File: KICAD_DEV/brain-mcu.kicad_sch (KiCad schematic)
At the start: 21 parts, among them SW1 SW_Push, SW2 SW_Push, U1 STM32H743VITx, Y1 8 MHz, Y2 32.768 KHz

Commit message: cleaning stuff up!
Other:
- note added: "IIf this SoC get's full, feel free to add a new one (just not too big!)"
- note added: "Please create a new hierarchial sheet in the root schematic, not this one if you're adding stuff!"
- note added: "Please don't alter anything aside from the GPIO's!"
- moved on the sheet: C10, C21, C23, C24, C25, C26, C27, C28, C29, C30, C31, C9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

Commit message: added all the basic footprints!
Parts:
- C10, C21, C23, C24, C25, C26, C27, C28, C29, C30, C31, C7, C8: footprint (none) -> Capacitor_SMD:C_0402_1005Metric
- C9: footprint (none) -> Capacitor_SMD:C_0603_1608Metric
- R13, R14: footprint (none) -> Resistor_SMD:R_0402_1005Metric
- SW1, SW2: footprint (none) -> Button_Switch_SMD:SW_Push_SPST_NO_Alps_SKRK
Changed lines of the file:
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@@
 			)
 		)
-		(property "Footprint" ""
+		(property "Footprint" "Capacitor_SMD:C_0603_1608Metric"
 			(at 55.5752 68.58 0)
 			(effects
@@
 			)
 		)
-		(property "Footprint" ""
+		(property "Footprint" "Capacitor_SMD:C_0402_1005Metric"
 			(at 77.1652 111.76 0)
 			(effects
@@
 			)
 		)
-		(property "Footprint" ""
+		(property "Footprint" "Capacitor_SMD:C_0402_1005Metric"
 			(at 192.7352 218.44 0)
 			(effects
@@
 			)
 		)
-		(property "Footprint" ""
+		(property "Footprint" "Button_Switch_SMD:SW_Push_SPST_NO_Alps_SKRK"
 			(at 68.58 97.79 0)
 			(effects
@@
 			)
 		)
-		(property "Footprint" ""
+		(property "Footprint" "Capacitor_SMD:C_0402_1005Metric"
 			(at 86.0552 68.58 0)
 			(effects
@@
 			)
 		)
-		(property "Footprint" ""
+		(property "Footprint" "Capacitor_SMD:C_0402_1005Metric"
 			(at 86.36 181.9148 0)
 			(effects
@@
 			)
 		)
-		(property "Footprint" ""
+		(property "Footprint" "Capacitor_SMD:C_0402_1005Metric"
 			(at 86.36 208.5848 0)
 			(effects
@@
 			)
 		)
-		(property "Footprint" ""
+		(property "Footprint" "Capacitor_SMD:C_0402_1005Metric"
 			(at 86.36 216.2048 0)
 			(effects
@@
 			)
 		)
-		(property "Footprint" ""
+		(property "Footprint" "Resistor_SMD:R_0402_1005Metric"
 			(at 74.422 143.51 90)
 			(effects
@@
 			)
 		)
-		(property "Footprint" ""
+		(property "Footprint" "Capacitor_SMD:C_0402_1005Metric"
 			(at 86.36 174.2948 0)
 			(effects
@@
 			)
 		)
-		(property "Footprint" ""
+		(property "Footprint" "Resistor_SMD:R_0402_1005Metric"
 			(at 74.422 97.79 90)
 			(effects
@@
 			)
 		)
-		(property "Footprint" ""
+		(property "Footprint" "Capacitor_SMD:C_0402_1005Metric"
 			(at 93.6752 68.58 0)
 			(effects
@@
 			)
 		)
-		(property "Footprint" ""
+		(property "Footprint" "Capacitor_SMD:C_0402_1005Metric"
 			(at 63.1952 68.58 0)
 			(effects
@@
 			)
 		)
-		(property "Footprint" ""
+		(property "Footprint" "Capacitor_SMD:C_0402_1005Metric"
 			(at 101.2952 68.58 0)
 			(effects
@@
 			)
 		)
-		(property "Footprint" ""
+		(property "Footprint" "Button_Switch_SMD:SW_Push_SPST_NO_Alps_SKRK"
 			(at 68.58 133.35 0)
 			(effects
@@
 			)
 		)
-		(property "Footprint" ""
+		(property "Footprint" "Capacitor_SMD:C_0402_1005Metric"
 			(at 78.4352 68.58 0)
 			(effects
@@
 			)
 		)
-		(property "Footprint" ""
+		(property "Footprint" "Capacitor_SMD:C_0402_1005Metric"
 			(at 70.8152 68.58 0)
 			(effects
@@
 			)
 		)
-		(property "Footprint" ""
+		(property "Footprint" "Capacitor_SMD:C_0402_1005Metric"
 			(at 185.1152 218.44 0)
 			(effects

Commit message: assigning more footprints!g
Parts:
- Y1: footprint (none) -> Crystal:Crystal_SMD_TXC_7A-2Pin_5x3.2mm; Part X49SM8MSD2SC -> X50328MSB2GI
- Y2: footprint (none) -> Crystal:Crystal_SMD_3215-2Pin_3.2x1.5mm
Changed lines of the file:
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@@
 			)
 		)
-		(property "Footprint" ""
+		(property "Footprint" "Crystal:Crystal_SMD_3215-2Pin_3.2x1.5mm"
 			(at 68.58 213.36 0)
 			(effects
@@
 			)
 		)
-		(property "Footprint" ""
+		(property "Footprint" "Crystal:Crystal_SMD_TXC_7A-2Pin_5x3.2mm"
 			(at 68.58 179.07 0)
 			(effects
@@
 			)
 		)
-		(property "Part" "X49SM8MSD2SC"
+		(property "Part" "X50328MSB2GI"
 			(at 68.58 173.228 90)
 			(effects

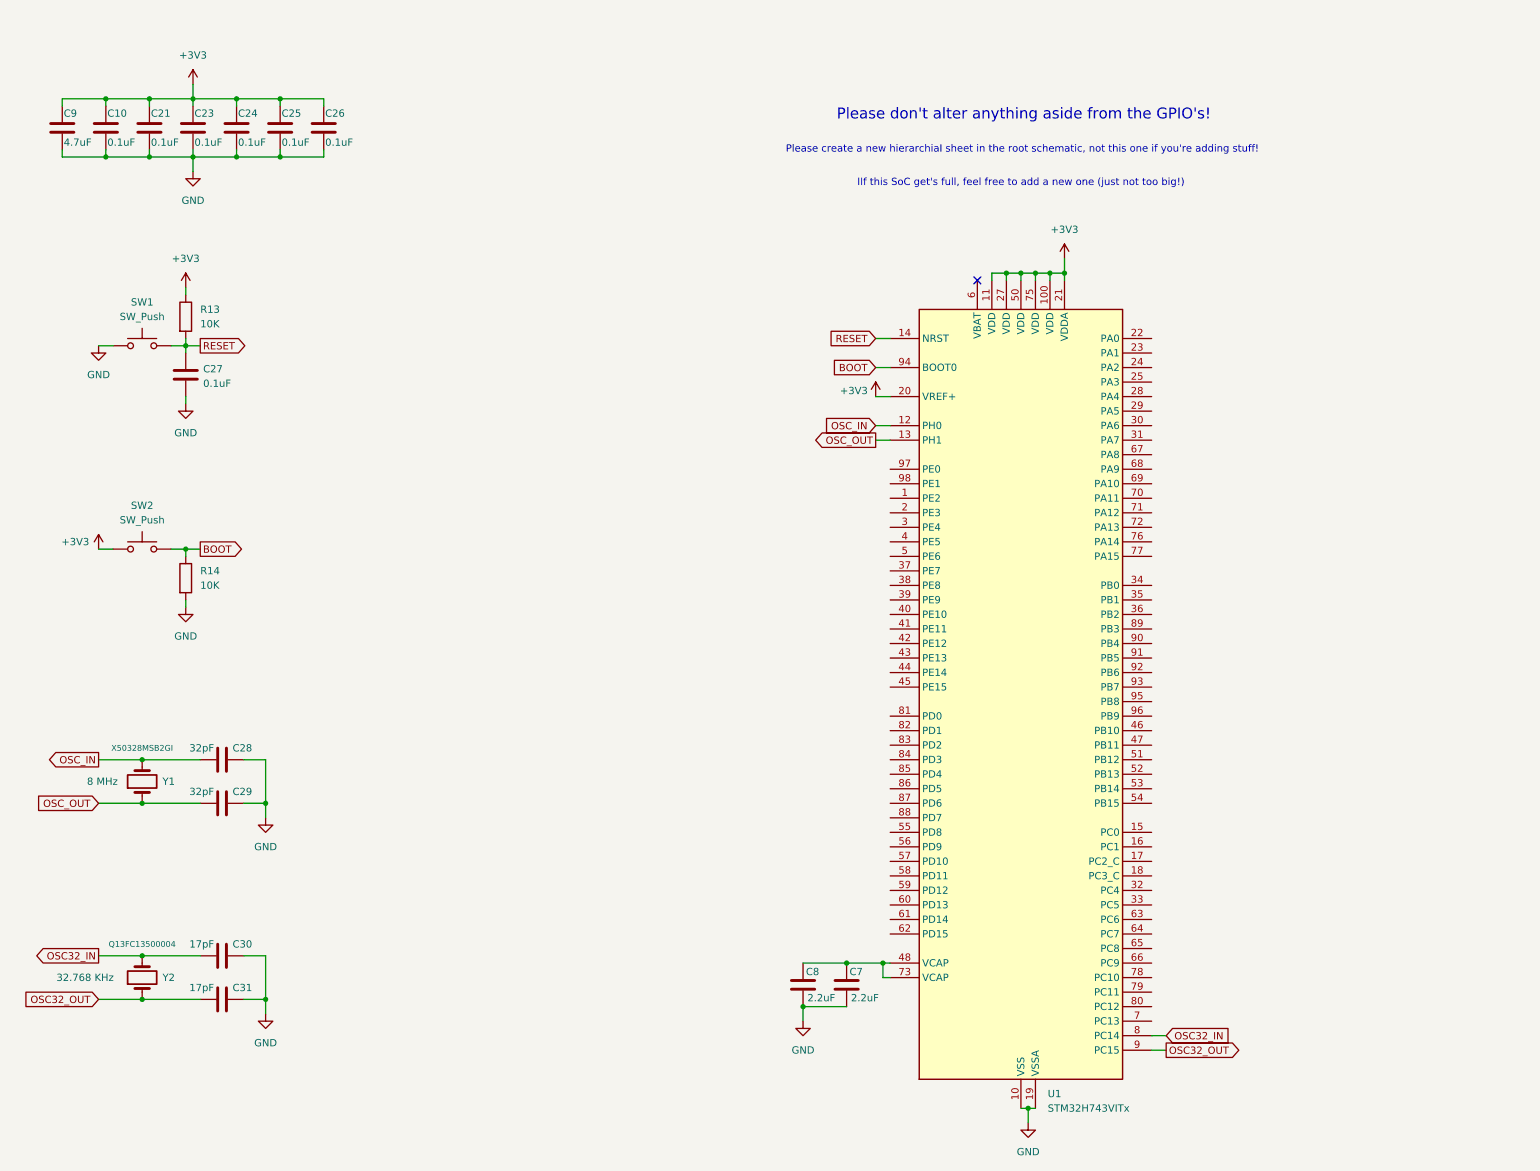
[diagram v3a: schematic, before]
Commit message: cleaning up the schematic, adding some footnotes for contributors!
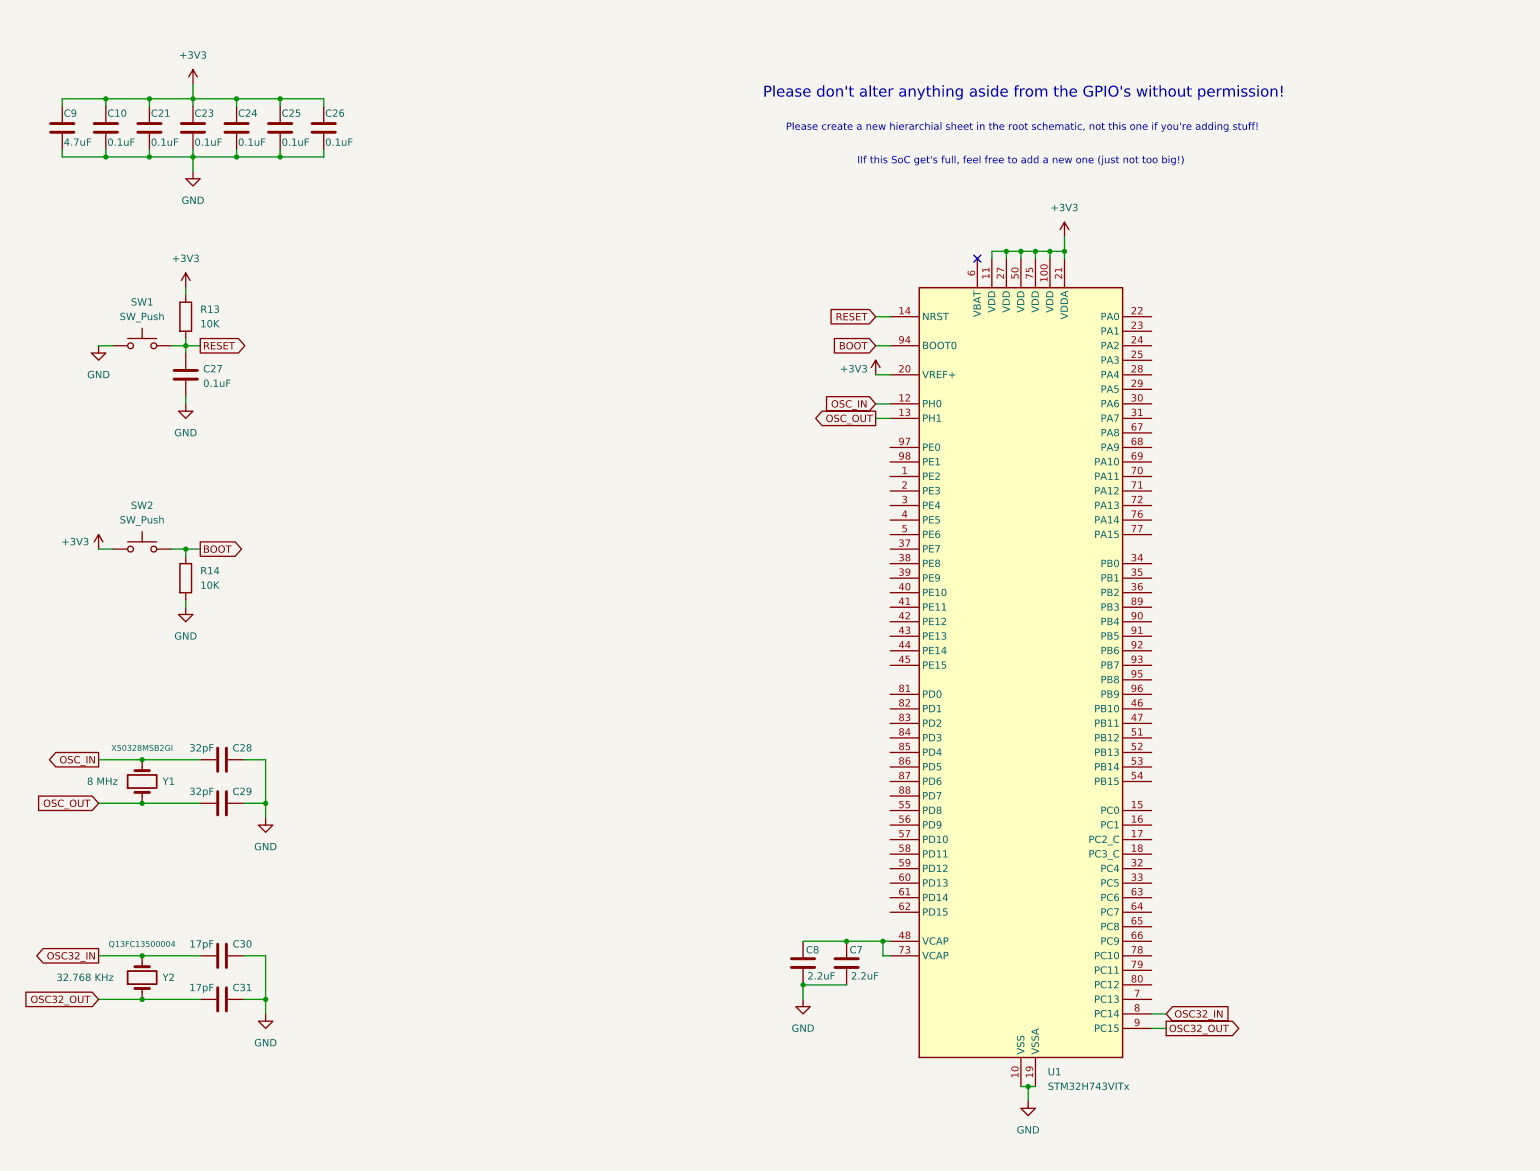
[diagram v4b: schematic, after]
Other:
- note added: "Please don't alter anything aside from the GPIO's without permission!"
- note removed: "Please don't alter anything aside from the GPIO's!"
- moved on the sheet: C7, C8, U1

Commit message: routed the SoC!
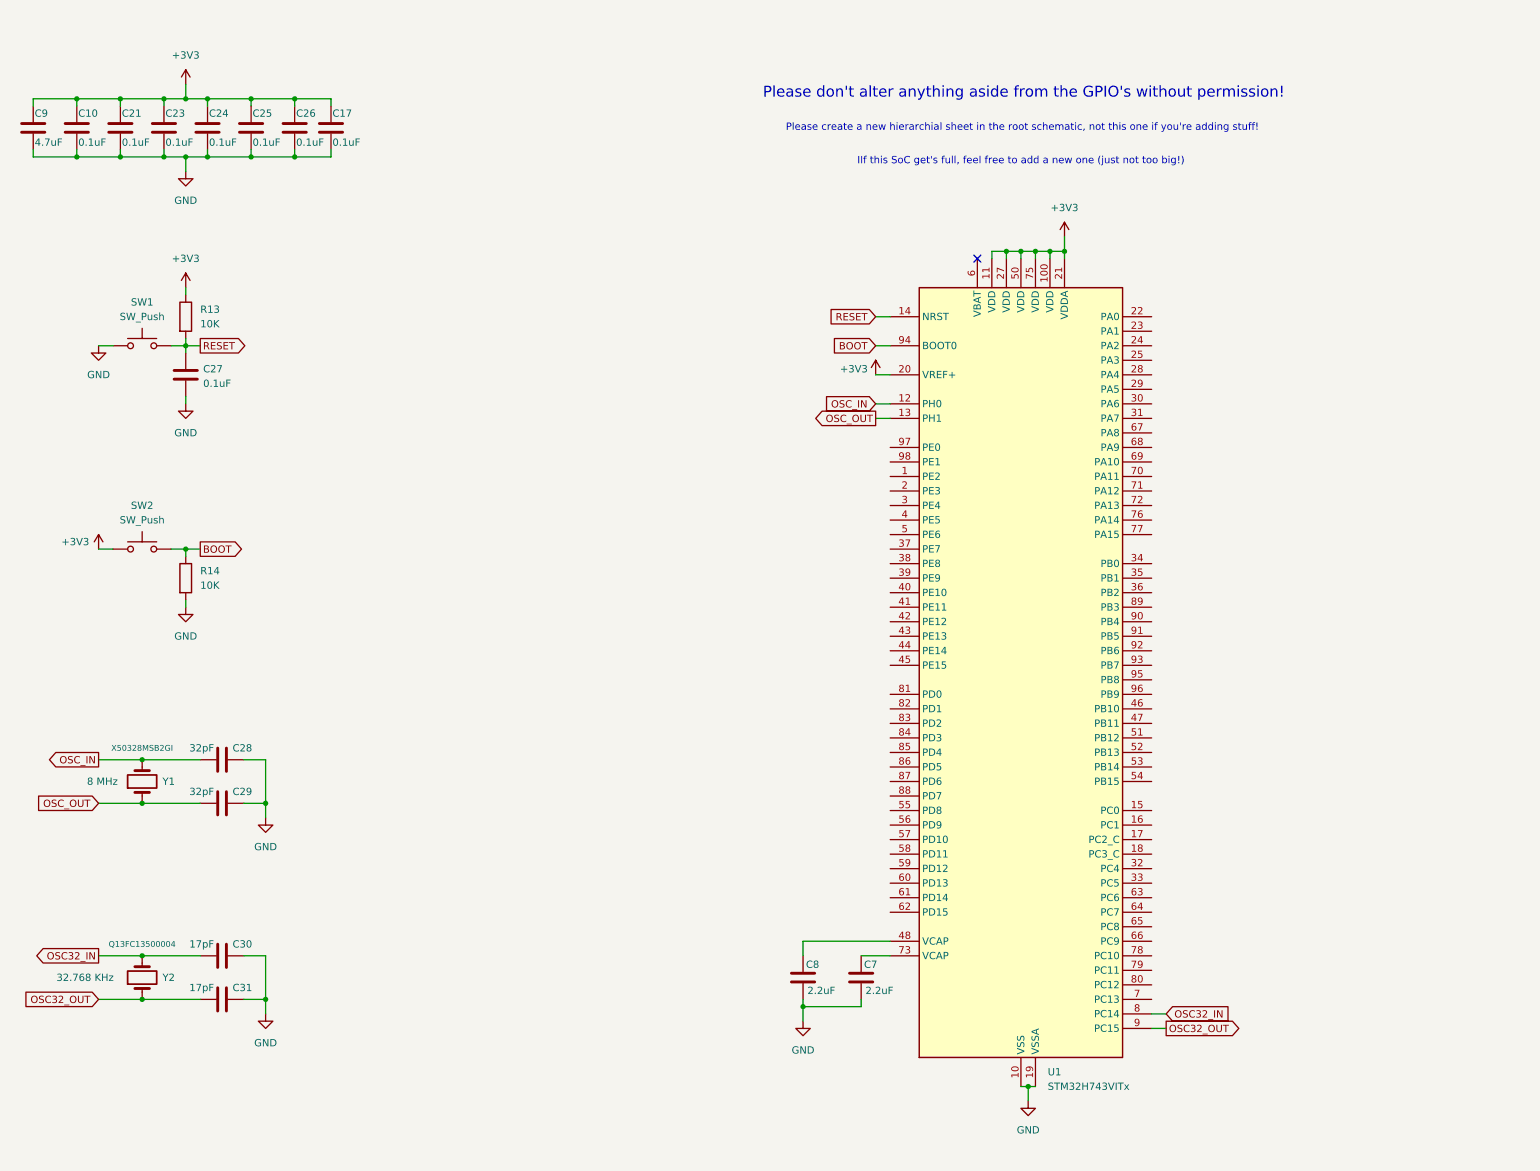
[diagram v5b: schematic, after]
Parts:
- added C17: 0.1uF, Capacitor_SMD:C_0402_1005Metric, symbol Device:C
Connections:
- net +3V3: now also C17.1
- net GND: now also C17.2
- net at C7.1, U1.73 (VCAP): no longer C8.1, U1.48 (VCAP)
- new net: C8.1, U1.48 (VCAP)
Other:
- moved on the sheet: C10, C21, C23, C24, C25, C26, C7, C8, C9

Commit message: forgot to wire USB data pairs, doing that now!
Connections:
- net D-: now reaches U1.70 (PA11)
- net D+: now reaches U1.71 (PA12)
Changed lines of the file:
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@@
+	(wire
+		(pts
+			(xy 247.65 128.27) (xy 245.11 128.27)
+		)
+		(stroke
+			(width 0)
+			(type default)
+		)
+	)
 	(wire
 		(pts
@@
 		(pts
 			(xy 76.2 148.59) (xy 76.2 147.32)
+		)
+		(stroke
+			(width 0)
+			(type default)
+		)
+	)
+	(wire
+		(pts
+			(xy 247.65 125.73) (xy 245.11 125.73)
 		)
 		(stroke
@@
 		)
 	)
+	(global_label "D-"
+		(shape input)
+		(at 247.65 125.73 0)
+		(fields_autoplaced yes)
+		(effects
+			(font
+				(size 1.27 1.27)
+			)
+			(justify left)
+		)
+		(property "Intersheetrefs" "${INTERSHEET_REFS}"
+			(at 253.4776 125.73 0)
+			(effects
+				(font
+					(size 1.27 1.27)
+				)
+				(justify left)
+				(hide yes)
+			)
+		)
+		(property "Netclass" "USB"
+			(at 247.65 127.9208 0)
+			(effects
+				(font
+					(size 1.27 1.27)
+				)
+				(justify left)
+				(hide yes)
+			)
+		)
+	)
 	(global_label "RESET"
 		(shape output)
@@
 			(effects
 				(font
+					(size 1.27 1.27)
+				)
+				(justify left)
+				(hide yes)
+			)
+		)
+	)
+	(global_label "D+"
+		(shape input)
+		(at 247.65 128.27 0)
+		(fields_autoplaced yes)
+		(effects
+			(font
+				(size 1.27 1.27)
+			)
+			(justify left)
+		)
+		(property "Intersheetrefs" "${INTERSHEET_REFS}"
+			(at 253.4776 128.27 0)
+			(effects
+				(font
+					(size 1.27 1.27)
+				)
+				(justify left)
+				(hide yes)
+			)
+		)
+		(property "Netclass" "USB"
+			(at 247.65 130.4608 0)
+			(effects
+				(font
